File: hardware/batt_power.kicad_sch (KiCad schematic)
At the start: 10 parts, among them J5 JST_PH_01x03, J6 Battery JST, Q1 AO3400A, U6 TPS7A2030PDBV

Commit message: Assigned resistor footprints
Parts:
- R5, R6, R7, R8: footprint (none) -> Resistor_SMD:R_0603_1608Metric_Pad0.98x0.95mm_HandSolder
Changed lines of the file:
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@@
 			)
 		)
-		(property "Footprint" ""
+		(property "Footprint" "Resistor_SMD:R_0603_1608Metric_Pad0.98x0.95mm_HandSolder"
 			(at 130.302 130.81 90)
 			(effects
@@
 			)
 		)
-		(property "Footprint" ""
+		(property "Footprint" "Resistor_SMD:R_0603_1608Metric_Pad0.98x0.95mm_HandSolder"
 			(at 115.57 144.018 90)
 			(effects
@@
 			)
 		)
-		(property "Footprint" ""
+		(property "Footprint" "Resistor_SMD:R_0603_1608Metric_Pad0.98x0.95mm_HandSolder"
 			(at 130.302 118.11 90)
 			(effects
@@
 			)
 		)
-		(property "Footprint" ""
+		(property "Footprint" "Resistor_SMD:R_0603_1608Metric_Pad0.98x0.95mm_HandSolder"
 			(at 120.142 148.59 90)
 			(effects

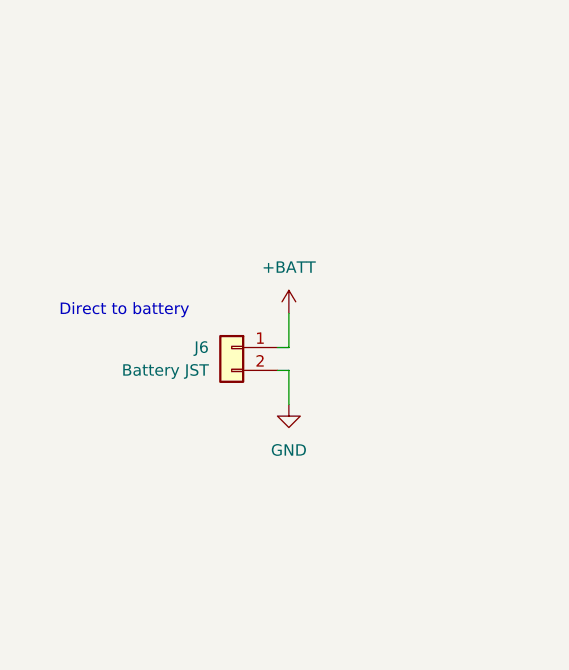
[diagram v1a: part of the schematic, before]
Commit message: Separated battery connector into 2 different
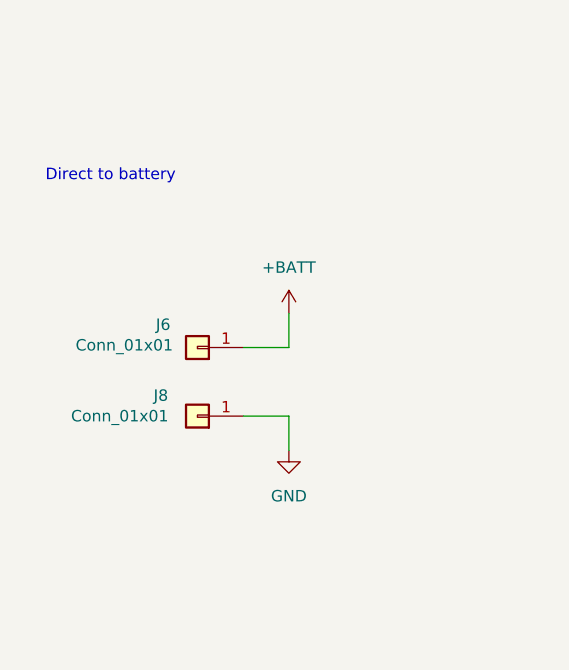
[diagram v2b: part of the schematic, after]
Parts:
- removed J6: Battery JST, Connector_Wire:SolderWire-1sqmm_1x02_P7.8mm_D1.4mm_OD3.9mm, symbol Connector_Generic:Conn_01x02
- added J6, J8: Conn_01x01, Connector_Wire:SolderWire-1sqmm_1x01_D1.4mm_OD3.9mm, symbol Connector_Generic:Conn_01x01
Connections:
- net +BATT: now also J6.1 (Pin_1)
- net GND: now also J8.1 (Pin_1)
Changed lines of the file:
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@@
-	(wire
-		(pts
-			(xy 59.69 82.55) (xy 60.96 82.55)
-		)
-		(stroke
-			(width 0)
-			(type default)
-		)
-	)
 	(wire
 		(pts
@@
 	(wire
 		(pts
+			(xy 55.88 80.01) (xy 60.96 80.01)
+		)
+		(stroke
+			(width 0)
+			(type default)
+		)
+	)
+	(wire
+		(pts
 			(xy 163.83 67.31) (xy 163.83 69.85)
 		)
@@
 	(wire
 		(pts
+			(xy 55.88 87.63) (xy 60.96 87.63)
+		)
+		(stroke
+			(width 0)
+			(type default)
+		)
+	)
+	(wire
+		(pts
 			(xy 132.08 121.92) (xy 132.08 124.46)
 		)
@@
 	(wire
 		(pts
-			(xy 60.96 82.55) (xy 60.96 86.36)
+			(xy 60.96 87.63) (xy 60.96 91.44)
 		)
 		(stroke
@@
 		(pts
 			(xy 140.97 58.42) (xy 170.18 58.42)
-		)
-		(stroke
-			(width 0)
-			(type default)
-		)
-	)
-	(wire
-		(pts
-			(xy 59.69 80.01) (xy 60.96 80.01)
 		)
 		(stroke
@@
 	(text "Direct to battery"
 		(exclude_from_sim no)
-		(at 42.672 75.946 0)
+		(at 41.148 60.96 0)
 		(effects
 			(font
@@
 	)
 	(symbol
+		(lib_id "Connector_Generic:Conn_01x01")
+		(at 50.8 87.63 180)
+		(unit 1)
+		(exclude_from_sim no)
+		(in_bom yes)
+		(on_board yes)
+		(dnp no)
+		(property "Reference" "J8"
+			(at 46.736 85.344 0)
+			(effects
+				(font
+					(size 1.27 1.27)
+				)
+			)
+		)
+		(property "Value" "Conn_01x01"
+			(at 42.164 87.63 0)
+			(effects
+				(font
+					(size 1.27 1.27)
+				)
+			)
+		)
+		(property "Footprint" "Connector_Wire:SolderWire-1sqmm_1x01_D1.4mm_OD3.9mm"
+			(at 50.8 87.63 0)
+			(effects
+				(font
+					(size 1.27 1.27)
+				)
+				(hide yes)
+			)
+		)
+		(property "Datasheet" "~"
+			(at 50.8 87.63 0)
+			(effects
+				(font
+					(size 1.27 1.27)
+				)
+				(hide yes)
+			)
+		)
+		(property "Description" "Generic connector, single row, 01x01, script generated (kicad-library-utils/schlib/autogen/connector/)"
+			(at 50.8 87.63 0)
+			(effects
+				(font
+					(size 1.27 1.27)
+				)
+				(hide yes)
+			)
+		)
+		(pin "1"
+		)
+		(instances
+			(project ""
+				(path "/c384ea46-0dfb-4673-b2f4-1f88fafbcaa5/f8f87cfe-571f-4a92-acee-79776e4ce004"
+					(reference "J8")
+					(unit 1)
+				)
+			)
+		)
+	)
+	(symbol
 		(lib_id "Transistor_FET:AO3400A")
 		(at 129.54 142.24 0)
@@
 	(symbol
 		(lib_id "power:GND")
-		(at 60.96 86.36 0)
+		(at 60.96 91.44 0)
 		(mirror y)
 		(unit 1)
@@
 		(fields_autoplaced yes)
 		(property "Reference" "#PWR046"
-			(at 60.96 92.71 0)
+			(at 60.96 97.79 0)
 			(effects
 				(font
@@
 		)
 		(property "Value" "GND"
+			(at 60.96 96.52 0)
+			(effects
+				(font
+					(size 1.27 1.27)
+				)
+			)
+		)
+		(property "Footprint" ""
 			(at 60.96 91.44 0)
 			(effects
@@
 					(size 1.27 1.27)
 				)
-			)
-		)
-		(property "Footprint" ""
-			(at 60.96 86.36 0)
-			(effects
-				(font
-					(size 1.27 1.27)
-				)
 				(hide yes)
 			)
 		)
 		(property "Datasheet" ""
-			(at 60.96 86.36 0)
+			(at 60.96 91.44 0)
 			(effects
 				(font
@@
 		)
 		(property "Description" "Power symbol creates a global label with name \"GND\" , ground"
-			(at 60.96 86.36 0)
+			(at 60.96 91.44 0)
 			(effects
 				(font
@@
 	)
 	(symbol
+		(lib_id "Connector_Generic:Conn_01x01")
+		(at 50.8 80.01 180)
+		(unit 1)
+		(exclude_from_sim no)
+		(in_bom yes)
+		(on_board yes)
+		(dnp no)
+		(property "Reference" "J6"
+			(at 46.99 77.47 0)
+			(effects
+				(font
+					(size 1.27 1.27)
+				)
+			)
+		)
+		(property "Value" "Conn_01x01"
+			(at 42.672 79.756 0)
+			(effects
+				(font
+					(size 1.27 1.27)
+				)
+			)
+		)
+		(property "Footprint" "Connector_Wire:SolderWire-1sqmm_1x01_D1.4mm_OD3.9mm"
+			(at 50.8 80.01 0)
+			(effects
+				(font
+					(size 1.27 1.27)
+				)
+				(hide yes)
+			)
+		)
+		(property "Datasheet" "~"
+			(at 50.8 80.01 0)
+			(effects
+				(font
+					(size 1.27 1.27)
+				)
+				(hide yes)
+			)
+		)
+		(property "Description" "Generic connector, single row, 01x01, script generated (kicad-library-utils/schlib/autogen/connector/)"
+			(at 50.8 80.01 0)
+			(effects
+				(font
+					(size 1.27 1.27)
+				)
+				(hide yes)
+			)
+		)
+		(pin "1"
+		)
+		(instances
+			(project ""
+				(path "/c384ea46-0dfb-4673-b2f4-1f88fafbcaa5/f8f87cfe-571f-4a92-acee-79776e4ce004"
+					(reference "J6")
+					(unit 1)
+				)
+			)
+		)
+	)
+	(symbol
 		(lib_id "Device:C")
 		(at 163.83 63.5 0)
@@
 					(unit 1)
 				)
-			)
-		)
-	)
-	(symbol
-		(lib_id "Connector_Generic:Conn_01x02")
-		(at 54.61 80.01 0)
-		(mirror y)
-		(unit 1)
-		(exclude_from_sim no)
-		(in_bom yes)
-		(on_board yes)
-		(dnp no)
-		(fields_autoplaced yes)
-		(property "Reference" "J6"
-			(at 52.07 80.0099 0)
-			(effects
-				(font
-					(size 1.27 1.27)
-				)
-				(justify left)
-			)
-		)
-		(property "Value" "Battery JST"
-			(at 52.07 82.5499 0)
-			(effects
-				(font
-					(size 1.27 1.27)
-				)
-				(justify left)
-			)
-		)
-		(property "Footprint" "Connector_Wire:SolderWire-1sqmm_1x02_P7.8mm_D1.4mm_OD3.9mm"
-			(at 54.61 80.01 0)
-			(effects
-				(font
-					(size 1.27 1.27)
-				)
-				(hide yes)
-			)
-		)
-		(property "Datasheet" "~"
-			(at 54.61 80.01 0)
-			(effects
-				(font
-					(size 1.27 1.27)
-				)
-				(hide yes)
-			)
-		)
-		(property "Description" "Generic connector, single row, 01x02, script generated (kicad-library-utils/schlib/autogen/connector/)"
-			(at 54.61 80.01 0)
-			(effects
-				(font
-					(size 1.27 1.27)
-				)
-				(hide yes)
-			)
-		)
-		(pin "1"
-		)
-		(pin "2"
-		)
-		(instances
-			(project ""
-				(path "/c384ea46-0dfb-4673-b2f4-1f88fafbcaa5/f8f87cfe-571f-4a92-acee-79776e4ce004"
-					(reference "J6")
-					(unit 1)
-				)
